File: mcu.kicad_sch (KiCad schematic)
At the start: 40 parts, among them J68 Conn_01x20, J69 Conn_01x20, J70 Socket_01x20, J71 Conn_01x20, J72 Conn_01x03, J73 Conn_01x03, J74 Conn_01x20, J75 Socket_01x20, J76 Conn_01x20, J77 Conn_01x20, U36 RPi_Pico_SMD_TH

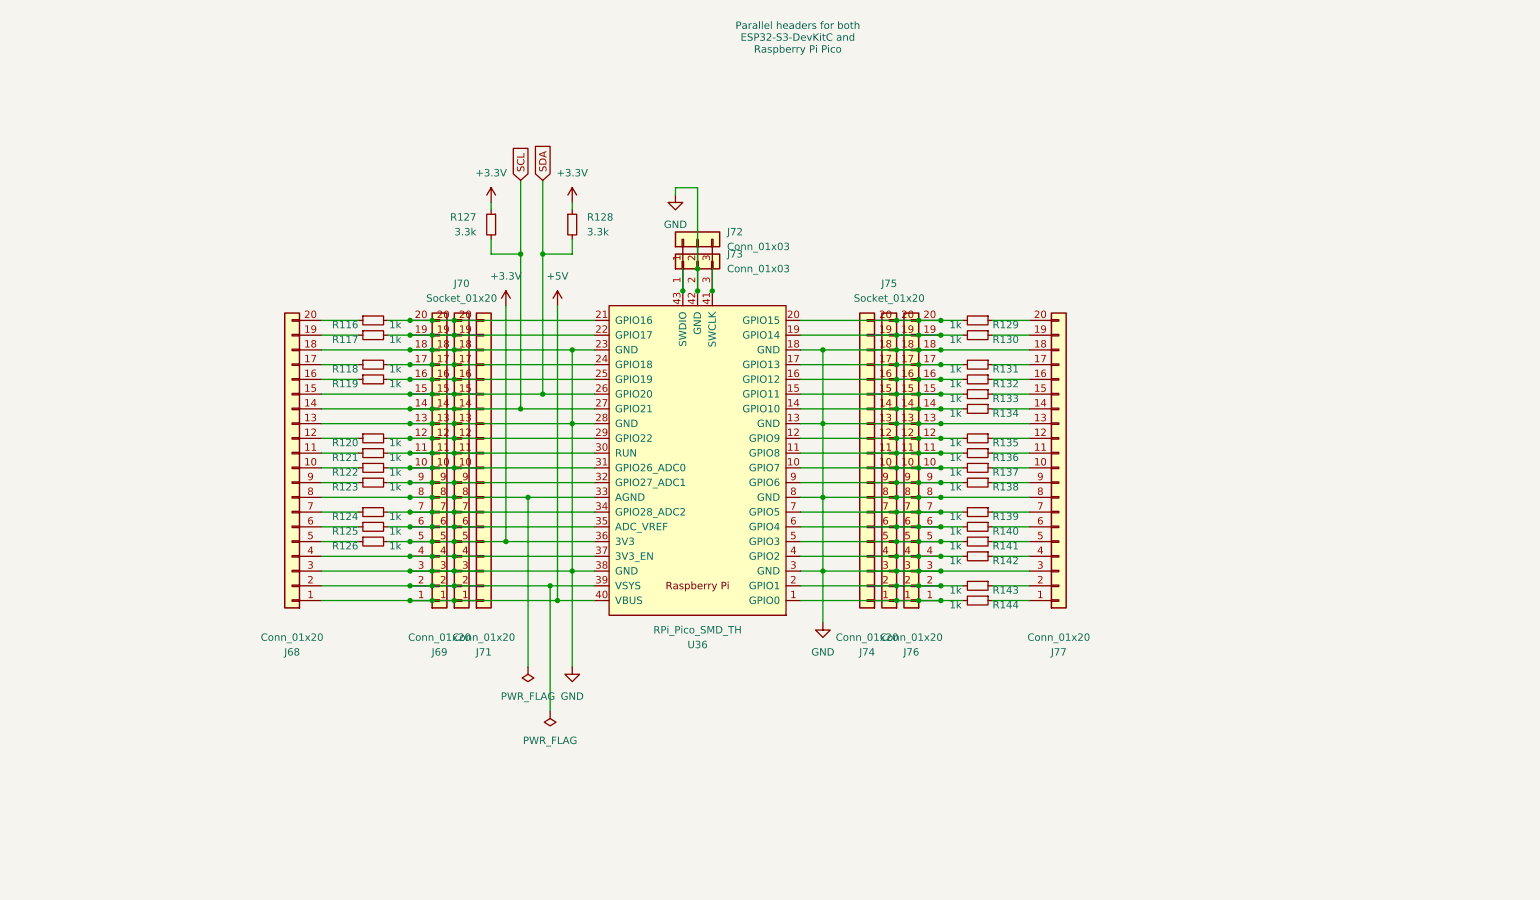
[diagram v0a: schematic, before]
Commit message: Update the design to a stackable one
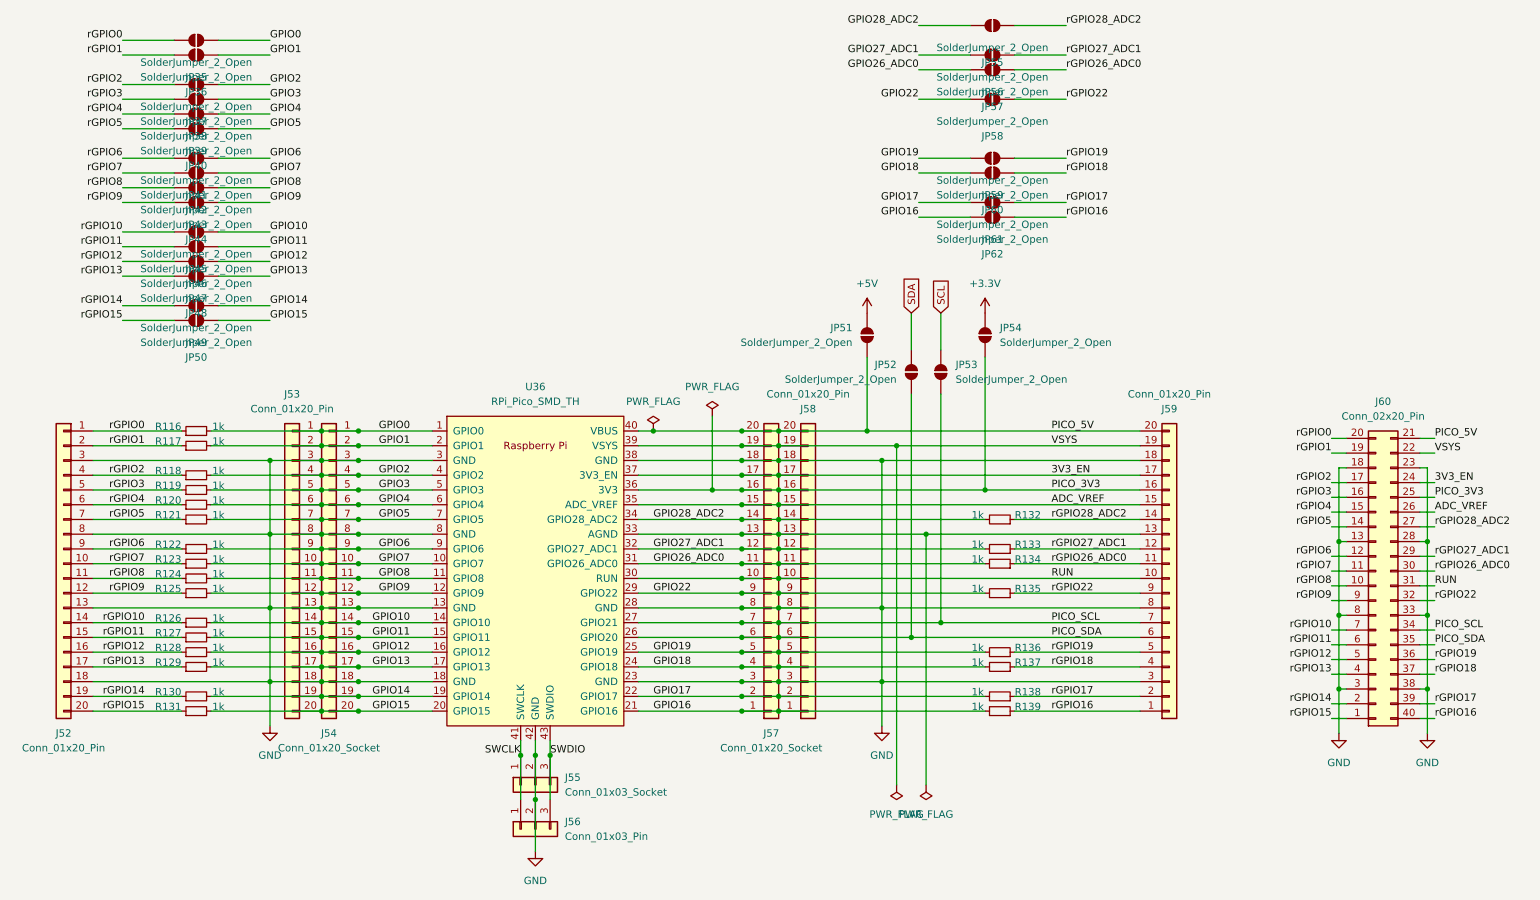
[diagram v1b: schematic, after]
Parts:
- removed J68, J69, J71, J74, J76, J77: Conn_01x20, HL_Connector_Pad_2.54mm:Pad_1x20_P2.54_1.7x1.7_Oct, symbol Connector_Generic:Conn_01x20
- removed J70, J75: Socket_01x20, HL_Connector_Pad_2.54mm:Pad_1x20_P2.54_1.7x1.7_Oct, symbol Connector_Generic:Conn_01x20
- removed J72, J73: Conn_01x03, HL_Connector_Pad_2.54mm:Pad_1x03_P2.54_1.7x1.7_Rnd-Rect-Rnd, symbol Connector_Generic:Conn_01x03
- removed R121, R125, R126: 1k, Resistor_SMD:R_0402_1005Metric, symbol Device:R_Small
- removed R127, R128: 3.3k, Resistor_SMD:R_0603_1608Metric, symbol Device:R_Small
- added J52, J53, J58, J59: Conn_01x20_Pin, HL_Connector_Pad_2.54mm:Pad_1x20_P2.54_1.7x1.7_Oct, symbol Connector_Generic:Conn_01x20
- added J54, J57: Conn_01x20_Socket, HL_Connector_Pad_2.54mm:Pad_1x20_P2.54_1.7x1.7_Oct, symbol Connector_Generic:Conn_01x20
- added J55: Conn_01x03_Socket, HL_Connector_Pad_2.54mm:Pad_1x03_P2.54_1.7x1.7_Oct-Rect-Oct, symbol Connector_Generic:Conn_01x03
- added J56: Conn_01x03_Pin, HL_Connector_Pad_2.54mm:Pad_1x03_P2.54_1.7x1.7_Oct-Rect-Oct, symbol Connector_Generic:Conn_01x03
- added J60: Conn_02x20_Pin, HL_Connector_Pad_2.54mm:Pad_2x20_P2.54_1.7x1.7_Pico, symbol Connector_Generic:Conn_02x20_Counter_Clockwise
- added JP35, JP36, JP37, JP38, JP39, JP40, JP41, JP42, JP43, JP44, JP45, JP46, JP47, JP48, JP49, JP50, JP51, JP52, JP53, JP54, JP55, JP56, JP57, JP58, JP59, JP60, JP61, JP62: SolderJumper_2_Open, Jumper:SolderJumper-2_P1.3mm_Open_TrianglePad1.0x1.5mm, symbol Jumper:SolderJumper_2_Open
- renumbered R144 to R116, R143 to R117, R142 to R118, R141 to R119, R140 to R120, R139 to R121, R138 to R122, R137 to R123, R136 to R124, R135 to R125, R134 to R126, R133 to R127, R132 to R128, R131 to R129, R129 to R131, R124 to R132, R123 to R133, R122 to R134, R120 to R135, R119 to R136, R118 to R137, R117 to R138, R116 to R139
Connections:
- net +3.3V: now also JP54.2 (B); no longer U36.36 (3V3)
- net +5V: now also JP51.2 (B); no longer U36.40 (VBUS)
- net GND: now also J52.13 (Pin_13), J52.18 (Pin_18), J52.3 (Pin_3), J52.8 (Pin_8), J53.13 (Pin_13), J53.18 (Pin_18), J53.3 (Pin_3), J53.8 (Pin_8), J54.13 (Pin_13), J54.18 (Pin_18), J54.3 (Pin_3), J54.8 (Pin_8), J55.2 (Pin_2), J56.2 (Pin_2), J57.18 (Pin_18), J57.3 (Pin_3), J57.8 (Pin_8), J58.18 (Pin_18), J58.3 (Pin_3), J58.8 (Pin_8), J59.18 (Pin_18), J59.3 (Pin_3), J59.8 (Pin_8), J60.13 (Pin_13), J60.18 (Pin_18), J60.23 (Pin_23), J60.28 (Pin_28), J60.3 (Pin_3), J60.33 (Pin_33), J60.38 (Pin_38), J60.8 (Pin_8)
- net SCL: now also JP53.2 (B); no longer U36.27 (GPIO21)
- net SDA: now also JP52.2 (B); no longer U36.26 (GPIO20)
- net GPIO0: now reaches R116.2, U36.1 (GPIO0)
- net GPIO0: now also J53.1 (Pin_1), J54.1 (Pin_1), JP35.1 (A)
- net GPIO7: now reaches R123.2, U36.10 (GPIO7)
- net GPIO7: now also J53.10 (Pin_10), J54.10 (Pin_10), JP42.1 (A)
- net GPIO8: now reaches R124.2, U36.11 (GPIO8)
- net GPIO8: now also J53.11 (Pin_11), J54.11 (Pin_11), JP43.1 (A)
- net GPIO9: now reaches R125.2, U36.12 (GPIO9)
- net GPIO9: now also J53.12 (Pin_12), J54.12 (Pin_12), JP44.1 (A)
- net GPIO10: now reaches R126.2, U36.14 (GPIO10)
- net GPIO10: now also J53.14 (Pin_14), J54.14 (Pin_14), JP45.1 (A)
- net GPIO11: now reaches R127.2, U36.15 (GPIO11)
- net GPIO11: now also J53.15 (Pin_15), J54.15 (Pin_15), JP46.1 (A)
- net GPIO12: now reaches R128.2, U36.16 (GPIO12)
- net GPIO12: now also J53.16 (Pin_16), J54.16 (Pin_16), JP47.1 (A)
- net GPIO13: now reaches R129.2, U36.17 (GPIO13)
- net GPIO13: now also J53.17 (Pin_17), J54.17 (Pin_17), JP48.1 (A)
- net GPIO14: now reaches R130.2, U36.19 (GPIO14)
- net GPIO14: now also J53.19 (Pin_19), J54.19 (Pin_19), JP49.1 (A)
- net GPIO1: now reaches R117.2, U36.2 (GPIO1)
- net GPIO1: now also J53.2 (Pin_2), J54.2 (Pin_2), JP36.1 (A)
- net GPIO15: now reaches R131.2, U36.20 (GPIO15)
- net GPIO15: now also J53.20 (Pin_20), J54.20 (Pin_20), JP50.1 (A)
- net GPIO2: now reaches R118.2, U36.4 (GPIO2)
- net GPIO2: now also J53.4 (Pin_4), J54.4 (Pin_4), JP37.1 (A)
- net GPIO3: now reaches R119.2, U36.5 (GPIO3)
- net GPIO3: now also J53.5 (Pin_5), J54.5 (Pin_5), JP38.1 (A)
- net GPIO4: now reaches R120.2, U36.6 (GPIO4)
- net GPIO4: now also J53.6 (Pin_6), J54.6 (Pin_6), JP39.1 (A)
- net GPIO5: now reaches R121.2, U36.7 (GPIO5)
- net GPIO5: now also J53.7 (Pin_7), J54.7 (Pin_7), JP40.1 (A)
- net GPIO6: now reaches R122.2, U36.9 (GPIO6)
- net GPIO6: now also J53.9 (Pin_9), J54.9 (Pin_9), JP41.1 (A)
- net GPIO26_ADC0: now reaches R134.2, U36.31 (GPIO26_ADC0)
- net GPIO26_ADC0: now also J57.11 (Pin_11), J58.11 (Pin_11), JP57.2 (B)
- net RUN: now reaches U36.30 (RUN)
- net RUN: now also J57.10 (Pin_10), J58.10 (Pin_10), J59.10 (Pin_10), J60.31 (Pin_31)
- net GPIO22: now reaches R135.2, U36.29 (GPIO22)
- net GPIO22: now also J57.9 (Pin_9), J58.9 (Pin_9), JP58.2 (B)
- net GPIO19: now reaches R136.2, U36.25 (GPIO19)
- net GPIO19: now also J57.5 (Pin_5), J58.5 (Pin_5), JP59.2 (B)
- net GPIO18: now reaches R137.2, U36.24 (GPIO18)
- net GPIO18: now also J57.4 (Pin_4), J58.4 (Pin_4), JP60.2 (B)
- net GPIO17: now reaches R138.2, U36.22 (GPIO17)
- net GPIO17: now also J57.2 (Pin_2), J58.2 (Pin_2), JP61.2 (B)
- net VSYS: now reaches U36.39 (VSYS)
- net VSYS: now also J57.19 (Pin_19), J58.19 (Pin_19), J59.19 (Pin_19), J60.22 (Pin_22)
- net GPIO16: now reaches R139.2, U36.21 (GPIO16)
- net GPIO16: now also J57.1 (Pin_1), J58.1 (Pin_1), JP62.2 (B)
- net 3V3_EN: now reaches U36.37 (3V3_EN)
- net 3V3_EN: now also J57.17 (Pin_17), J58.17 (Pin_17), J59.17 (Pin_17), J60.24 (Pin_24)
- net ADC_VREF: now reaches U36.35 (ADC_VREF)
- net ADC_VREF: now also J57.15 (Pin_15), J58.15 (Pin_15), J59.15 (Pin_15), J60.26 (Pin_26)
- net GPIO28_ADC2: now reaches R132.2, U36.34 (GPIO28_ADC2)
- net GPIO28_ADC2: now also J57.14 (Pin_14), J58.14 (Pin_14), JP55.2 (B)
- net at U36.33 (AGND): now also J57.13 (Pin_13), J58.13 (Pin_13), J59.13 (Pin_13)
- net GPIO27_ADC1: now reaches R133.2, U36.32 (GPIO27_ADC1)
- net GPIO27_ADC1: now also J57.12 (Pin_12), J58.12 (Pin_12), JP56.2 (B)
- net rGPIO12: now reaches R128.1
- net rGPIO12: now also J52.16 (Pin_16), J60.5 (Pin_5), JP47.2 (B)
- net rGPIO0: now reaches R116.1
- net rGPIO0: now also J52.1 (Pin_1), J60.20 (Pin_20), JP35.2 (B)
- net rGPIO16: now reaches R139.1
- net rGPIO16: now also J59.1 (Pin_1), J60.40 (Pin_40), JP62.1 (A)
- net rGPIO7: now reaches R123.1
- net rGPIO7: now also J52.10 (Pin_10), J60.11 (Pin_11), JP42.2 (B)
- net rGPIO8: now reaches R124.1
- net rGPIO8: now also J52.11 (Pin_11), J60.10 (Pin_10), JP43.2 (B)
- net rGPIO9: now reaches R125.1
- net rGPIO9: now also J52.12 (Pin_12), J60.9 (Pin_9), JP44.2 (B)
- net rGPIO10: now reaches R126.1
- net rGPIO10: now also J52.14 (Pin_14), J60.7 (Pin_7), JP45.2 (B)
- net rGPIO11: now reaches R127.1
- net rGPIO11: now also J52.15 (Pin_15), J60.6 (Pin_6), JP46.2 (B)
- net rGPIO13: now reaches R129.1
- net rGPIO13: now also J52.17 (Pin_17), J60.4 (Pin_4), JP48.2 (B)
- net rGPIO14: now reaches R130.1
- net rGPIO14: now also J52.19 (Pin_19), J60.2 (Pin_2), JP49.2 (B)
- net rGPIO1: now reaches R117.1
- net rGPIO1: now also J52.2 (Pin_2), J60.19 (Pin_19), JP36.2 (B)
- net rGPIO15: now reaches R131.1
- net rGPIO15: now also J52.20 (Pin_20), J60.1 (Pin_1), JP50.2 (B)
- net rGPIO2: now reaches R118.1
- net rGPIO2: now also J52.4 (Pin_4), J60.17 (Pin_17), JP37.2 (B)
- net rGPIO3: now reaches R119.1
- net rGPIO3: now also J52.5 (Pin_5), J60.16 (Pin_16), JP38.2 (B)
- net rGPIO4: now reaches R120.1
- net rGPIO4: now also J52.6 (Pin_6), J60.15 (Pin_15), JP39.2 (B)
- net rGPIO5: now reaches R121.1
- net rGPIO5: now also J52.7 (Pin_7), J60.14 (Pin_14), JP40.2 (B)
- net rGPIO6: now reaches R122.1
- net rGPIO6: now also J52.9 (Pin_9), J60.12 (Pin_12), JP41.2 (B)
- net rGPIO28_ADC2: now reaches R132.1
- net rGPIO28_ADC2: now also J59.14 (Pin_14), J60.27 (Pin_27), JP55.1 (A)
- net rGPIO19: now reaches R136.1
- net rGPIO19: now also J59.5 (Pin_5), J60.36 (Pin_36), JP59.1 (A)
- net SWDIO: now reaches U36.43 (SWDIO)
- net SWDIO: now also J55.3 (Pin_3), J56.3 (Pin_3)
- net SWCLK: now reaches U36.41 (SWCLK)
- net SWCLK: now also J55.1 (Pin_1), J56.1 (Pin_1)
- net rGPIO17: now reaches R138.1
- net rGPIO17: now also J59.2 (Pin_2), J60.39 (Pin_39), JP61.1 (A)
- net rGPIO22: now reaches R135.1
- net rGPIO22: now also J59.9 (Pin_9), J60.32 (Pin_32), JP58.1 (A)
- net rGPIO26_ADC0: now reaches R134.1
- net rGPIO26_ADC0: now also J59.11 (Pin_11), J60.30 (Pin_30), JP57.1 (A)
- net rGPIO18: now reaches R137.1
- net rGPIO18: now also J59.4 (Pin_4), J60.37 (Pin_37), JP60.1 (A)
- net rGPIO27_ADC1: now reaches R133.1
- net rGPIO27_ADC1: now also J59.12 (Pin_12), J60.29 (Pin_29), JP56.1 (A)
- new net PICO_3V3: J57.16 (Pin_16), J58.16 (Pin_16), J59.16 (Pin_16), J60.25 (Pin_25), JP54.1 (A), U36.36 (3V3)
- new net PICO_5V: J57.20 (Pin_20), J58.20 (Pin_20), J59.20 (Pin_20), J60.21 (Pin_21), JP51.1 (A), U36.40 (VBUS)
- new net PICO_SCL: J57.7 (Pin_7), J58.7 (Pin_7), J59.7 (Pin_7), J60.34 (Pin_34), JP53.1 (A), U36.27 (GPIO21)
- new net PICO_SDA: J57.6 (Pin_6), J58.6 (Pin_6), J59.6 (Pin_6), J60.35 (Pin_35), JP52.1 (A), U36.26 (GPIO20)
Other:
- note removed: "Parallel headers for both ESP32-S3-DevKitC and Raspberry Pi Pico"
- moved on the sheet: R116, R117, R118, R119, R120, R121, R122, R123, R124, R125, R126, R127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
